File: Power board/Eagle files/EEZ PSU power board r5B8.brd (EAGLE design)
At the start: 74 x 150 mm, 270 parts, among them IC1 LTC3864, IC10 REF5025, IC11 DAC8552, IC12 ADG465SOT-23, IC13 TS5A9411DCKT, IC14 ADS1120, IC15 LP339D, IC2 MC79L05, IC3 MC78L05, IC4 LM5574, IC5 LP2951SO8, IC6 TL072D, IC7 TL072D, IC8 OP27GSZ, IC9 MCP23S08-E/SO, Q1 SUD19P06-60, Q10 MMBT5401, Q11 MMBT5401, Q12 MMBT5551, Q13 MMBT5551, Q14 BSS84P, Q15 2N7002, Q16 MMBT5551, Q17 MMBT5401, Q18 MMBT5551, Q19 MMBT5551, Q2 MMBT5401, Q3 2N7002, Q4 IRFP250N, Q5 BC857C, Q6 BC846C, Q7 BCP56-16.115, Q8 IRFR5410, Q9 BCP56-16.115, X1 282836-3, X2 282836-2, X3 SSW-113-02-T-D-RA

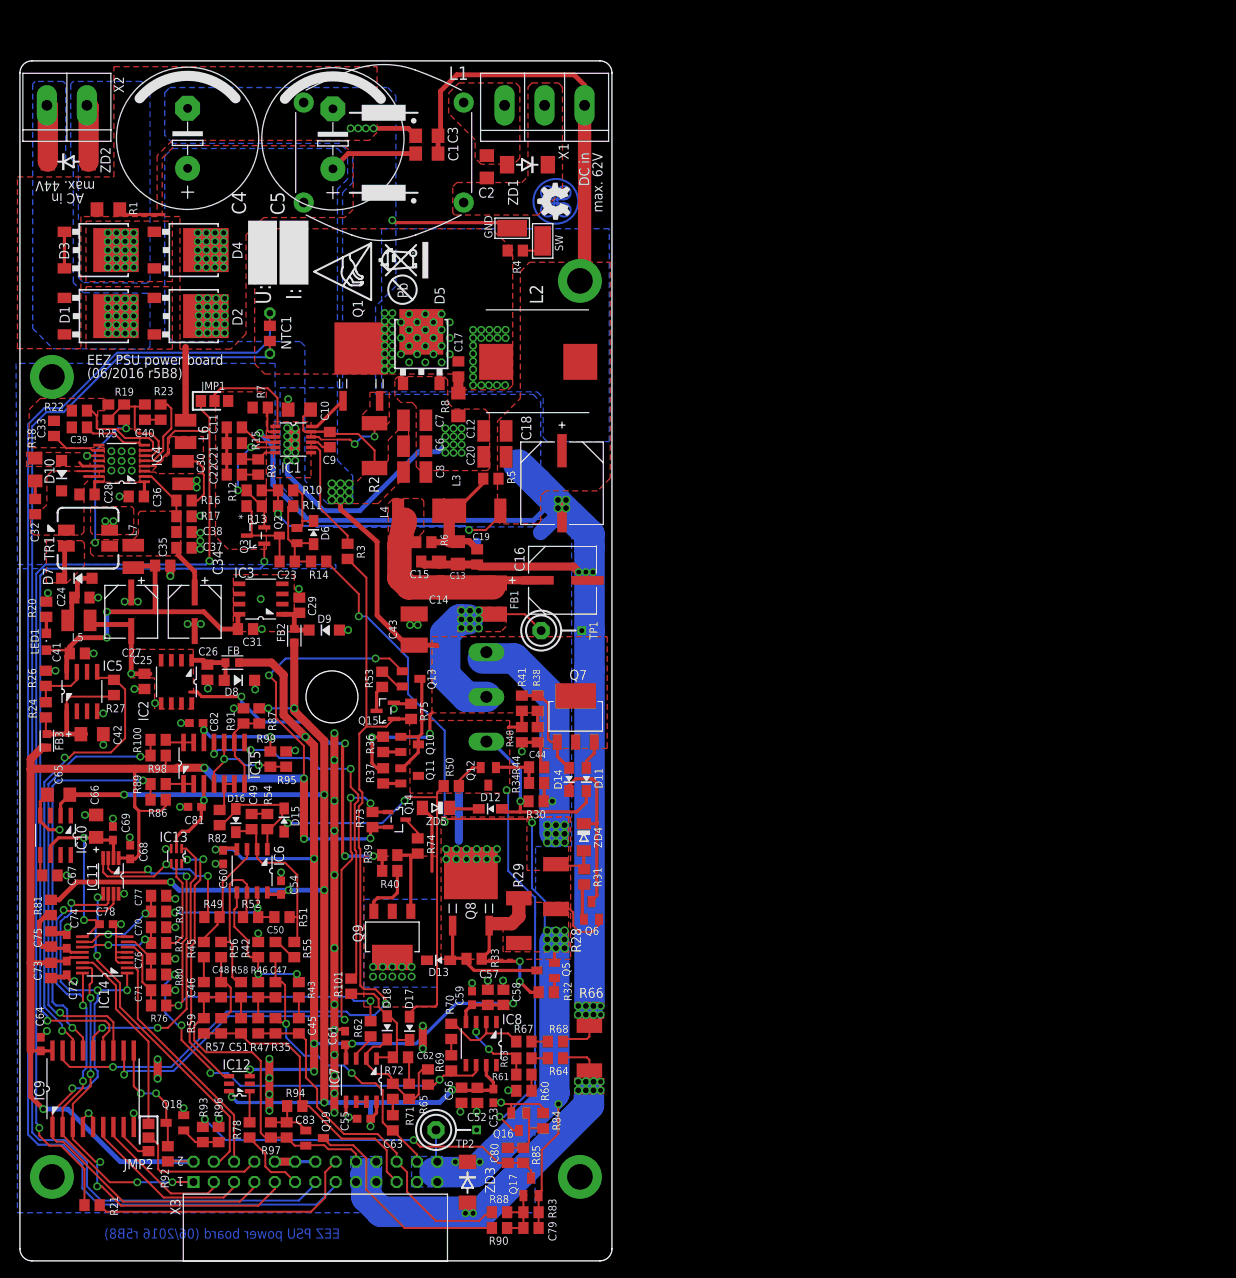
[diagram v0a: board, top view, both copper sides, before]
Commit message: Power board PCB layout and BOM changes
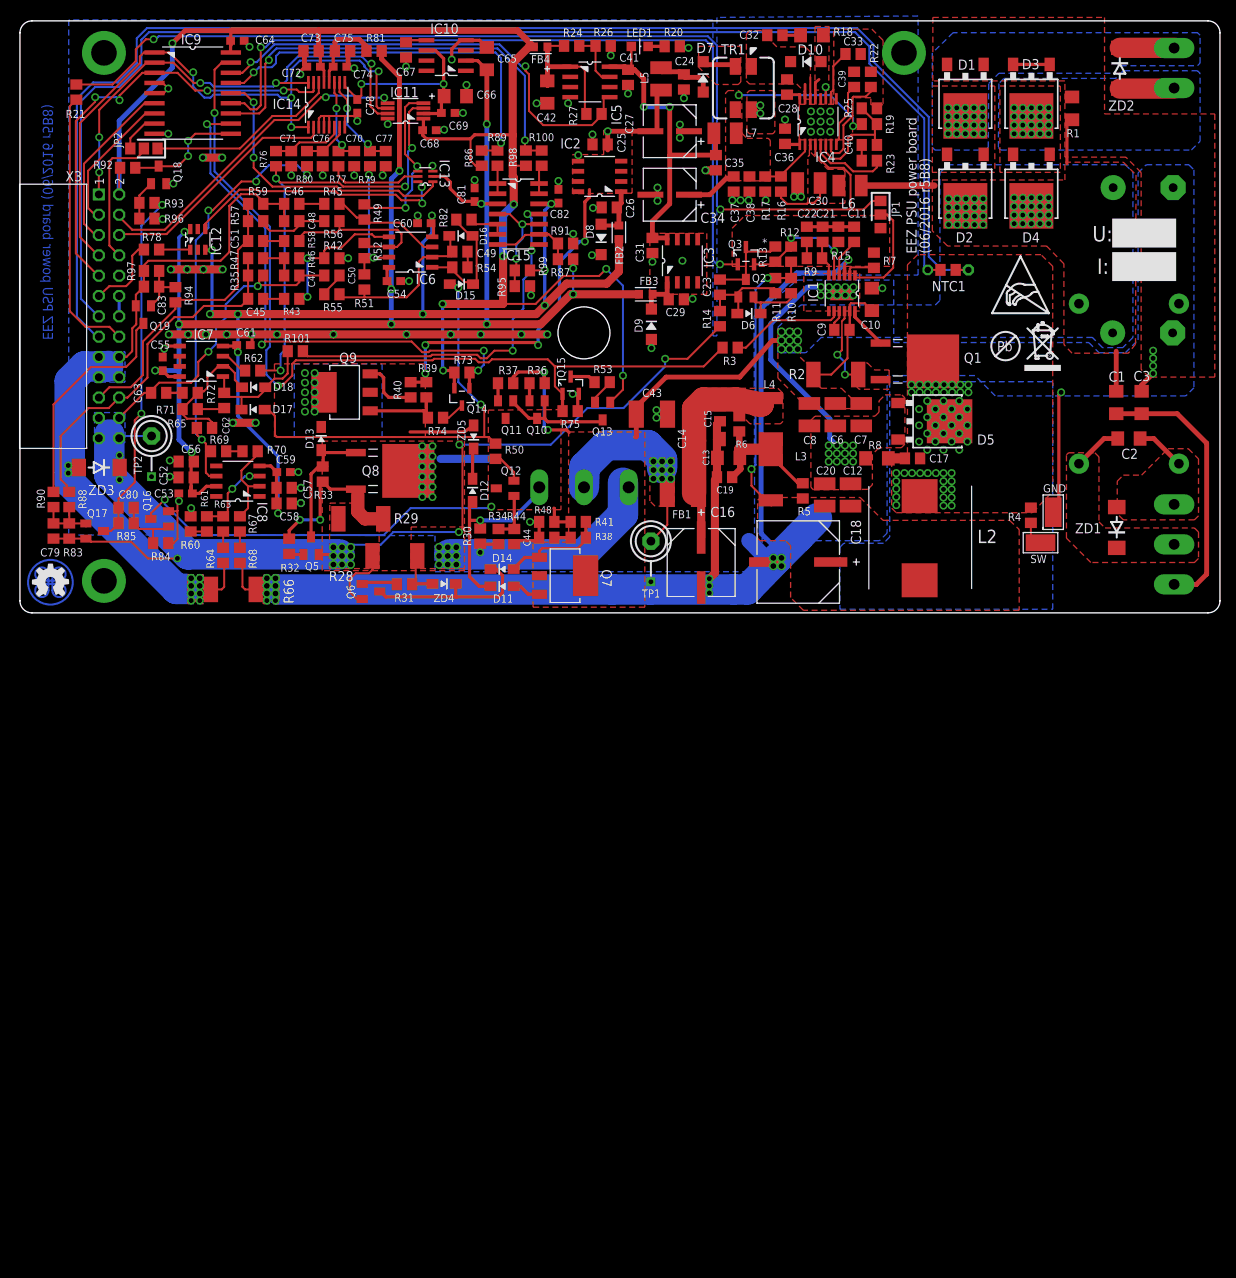
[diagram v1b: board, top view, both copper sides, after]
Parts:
- removed FB: 60R@100MHz, EEZ_Lib1:BEAD0603
- removed JMP1, JMP2: 0R-JUMPA, jump-0r-smd:A0R-JMP
- added FB4: 60R@100MHz, EEZ_Lib1:BEAD0603
- added JP1, JP2: 0R-JUMPA, jump-0r-smd:A0R-JMP
- C18: value EEEFK1J470P -> EEEFK1J101P
- D5: device EEZ_Lib1:TO252@1 -> EEZ_Lib1:TO252
- L2: value See Note 1.2 -> 7443551331
- LED1: device led:CHIPLED_0805 -> EEZ_Lib1:LED_0805
- R12: value See Note 1.3 -> 324K
- ZD4: value 13V -> BZX384-C15.115; device EEZ_Lib1:MINIMELF -> EEZ_Lib1:SOD323-W
- ZD5: value 6V2 -> PDZ6.2B; device EEZ_Lib1:MINIMELF -> EEZ_Lib1:SOD323-W
- moved X2 140.9 mm to (144.3, 141.6), flipped to the bottom, turned to 180 degrees
- moved R21 139.1 mm to (7.05, 141.1), turned to 270 degrees
- moved ZD2 132.0 mm to (137.5, 144.1), turned to 270 degrees
- moved C64 127.8 mm to (27.2, 147.5), turned to 0 degrees
- moved IC9 125.1 mm to (21.6, 141.0), turned to 0 degrees
- moved R92 123.4 mm to (13.5, 131.6), turned to 180 degrees
- moved R1 121.1 mm to (131.5, 139.1), turned to 90 degrees
- moved C4 119.6 mm to (140.4, 129.2), flipped to the bottom, turned to 180 degrees
- moved C73 119.4 mm to (36.4, 146.2), turned to 0 degrees
- moved Q18 118.5 mm to (17.3, 130.7), turned to 0 degrees
- moved C75 116.8 mm to (40.3, 146.2), turned to 180 degrees
- moved C72 116.8 mm to (36.7, 144.3), turned to 0 degrees
- moved D3 116.7 mm to (126.4, 139.1), turned to 180 degrees
- moved R93 116.7 mm to (15.9, 127.3), turned to 0 degrees
- moved R96 114.8 mm to (15.9, 125.3), turned to 180 degrees
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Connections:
- net !INT: now also JP2.2; no longer JMP2.2
- net !PS_DRDY: now also JP2.3; no longer JMP2.3
- net +5V: now also FB4.P$2; no longer FB3.P$2
- net AC_IN1: now also X2.1; no longer X2.2
- net AC_IN2: now also X2.2; no longer X2.1
- net DC+: now also L1.2; no longer L1.1
- net DC-: now also L1.1, X1.3; no longer L1.2, X1.1
- net DC_OUT: now also L1.3; no longer L1.4
- net EARTH: now also X1.1; no longer X1.3
- net GND: now also L1.4; no longer L1.3
- net INT_EXP: now also JP2.1; no longer JMP2.1
- net MODE: now also JP1.2; no longer JMP1.2
- net N$4: now also FB2.P$1; no longer FB.P$1
- net N$5: now also FB3.P$1; no longer FB2.P$1
- net N$6: now also FB4.P$1; no longer FB3.P$1
- net SGND: now also JP1.1; no longer JMP1.1
- net SYNC: now also JP1.3; no longer JMP1.3
- net V+: now also FB3.P$2; no longer FB2.P$2
- net V-: now also FB2.P$2; no longer FB.P$2
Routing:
- net EARTH: track 52.0 -> 33.8 mm, vias 1 -> 0
- net DC-: track 0.00 -> 6.15 mm
- net DC+: track 0.00 -> 6.15 mm
- net DC_OUT: track 84.2 -> 78.1 mm
- net GND: track 247.2 -> 241.5 mm
- net POUT-: track 107.6 -> 110.7 mm
- net AUX_USET_IN: track 9.05 -> 9.89 mm
- net +5V: track 189.5 -> 188.9 mm
- net Q4_OUT: track 41.6 -> 42.1 mm
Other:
- board size 74 x 150 mm -> 150 x 74 mm
- board text added: "AC in 1"
- board text added: "AC in 2"
- board text added: "AC input X2"
- board text added: "DC in max. 62V"
- board text added: "DC in+ 2"
- board text added: "DC in- 1"
- board text added: "DC input X1"
- board text added: "Earth 3"
- board text added: "FB4"
- board text added: "JP1"
- board text added: "JP2"
- board text removed: "DC in"
- board text removed: "FB"
- board text removed: "JMP1"
- board text removed: "JMP2"
- board text removed: "Licensed under the TAPR Open Hardware License (www.tapr.org/OHL)"
- board text removed: "max. 62V"

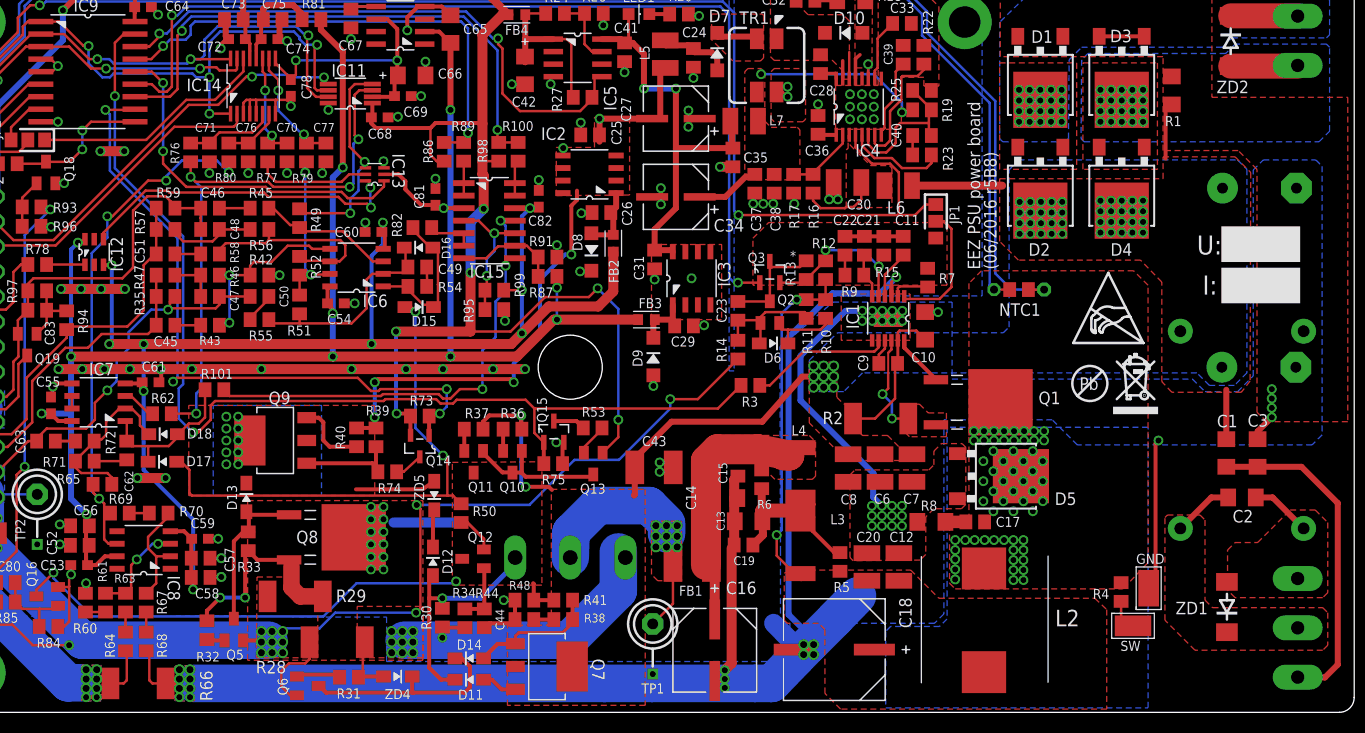
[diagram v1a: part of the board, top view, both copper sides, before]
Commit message: Missed hole added to Power board, minor bottom silk mask changes
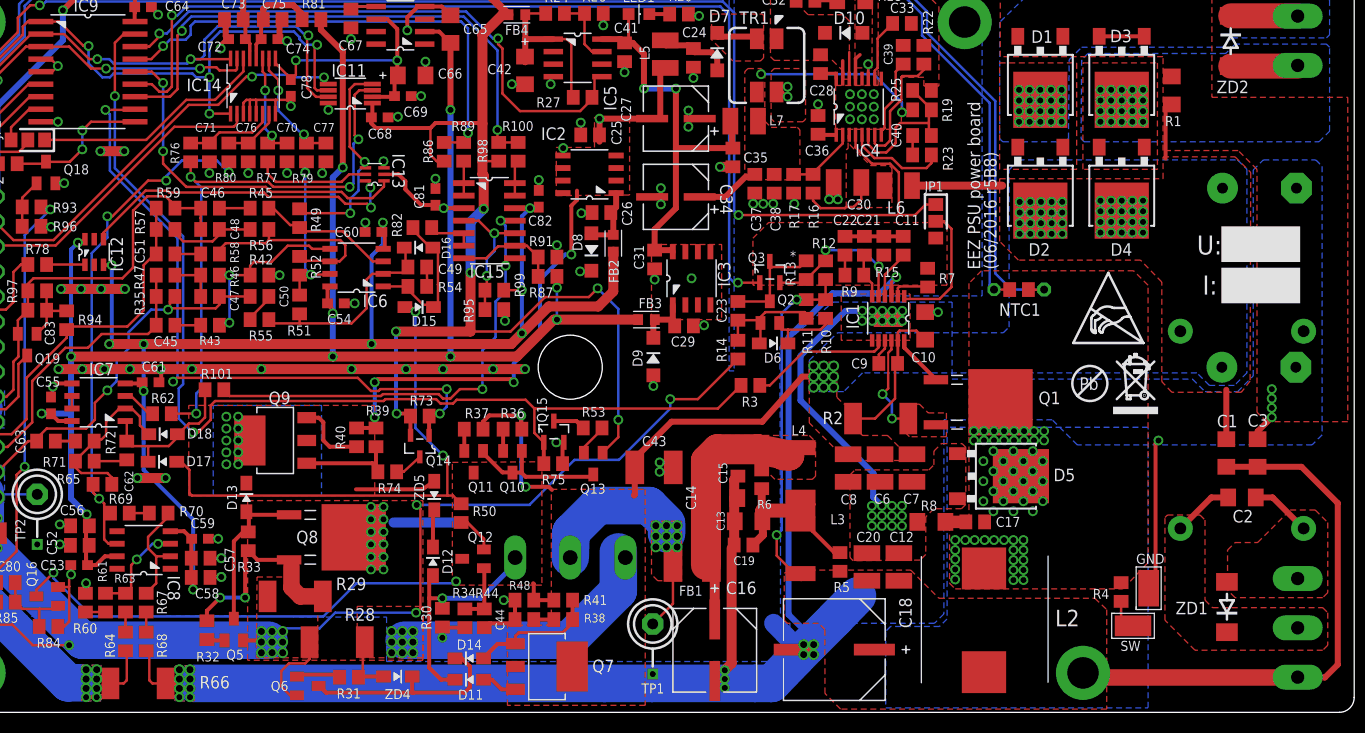
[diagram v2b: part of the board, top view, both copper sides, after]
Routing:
- net EARTH: track 33.8 -> 55.8 mm, vias 0 -> 1

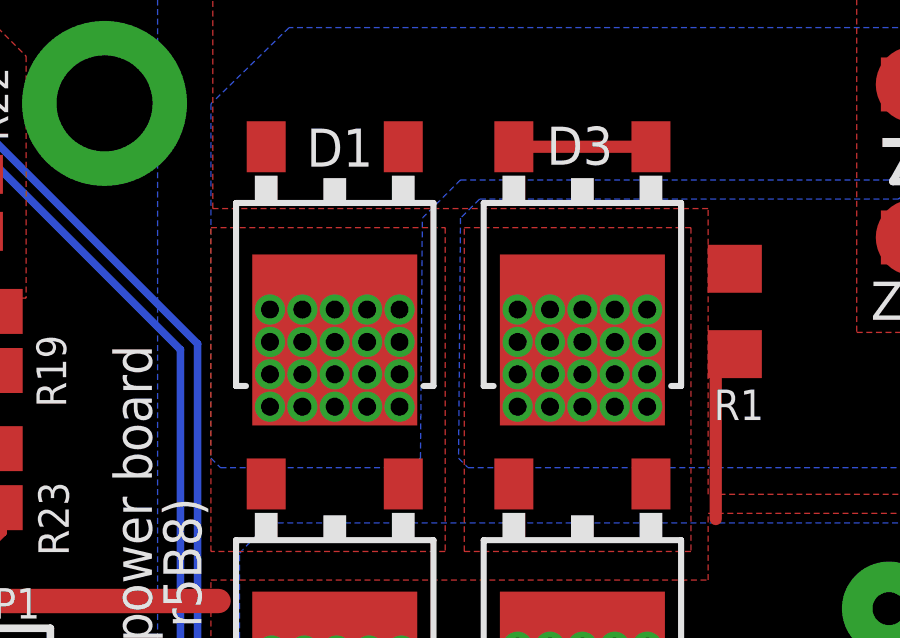
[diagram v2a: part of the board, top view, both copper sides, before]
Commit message: Consolidated BOM for PCBA, AUX PS BOM update, Power module PCB update
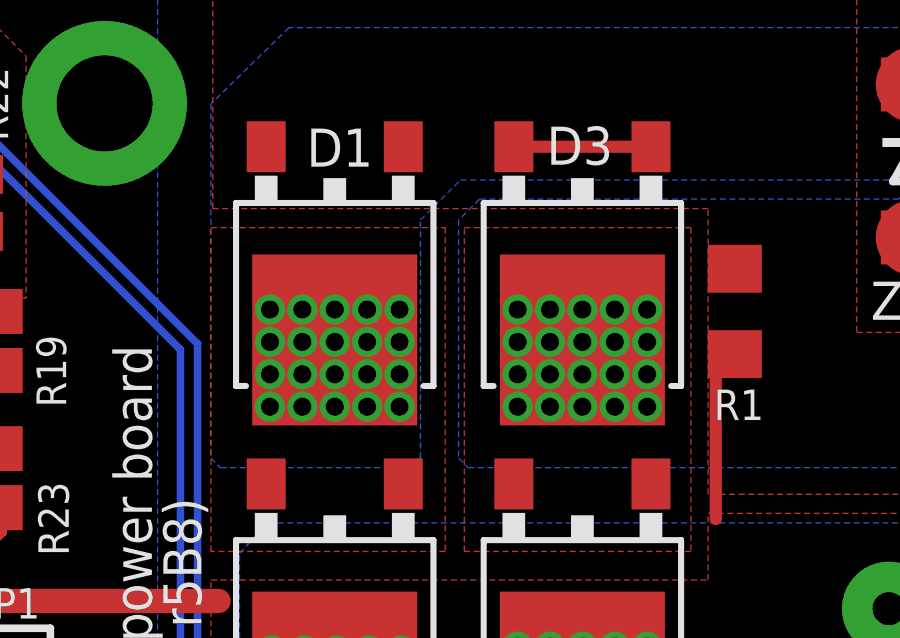
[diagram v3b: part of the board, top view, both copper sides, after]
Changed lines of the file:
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@@
 <layer number="27" name="tValues" color="10" fill="1" visible="no" active="yes"/>
 <layer number="28" name="bValues" color="11" fill="1" visible="no" active="yes"/>
-<layer number="29" name="tStop" color="7" fill="3" visible="no" active="yes"/>
-<layer number="30" name="bStop" color="7" fill="6" visible="yes" active="yes"/>
+<layer number="29" name="tStop" color="7" fill="3" visible="yes" active="yes"/>
+<layer number="30" name="bStop" color="7" fill="6" visible="no" active="yes"/>
 <layer number="31" name="tCream" color="7" fill="4" visible="no" active="yes"/>
 <layer number="32" name="bCream" color="7" fill="5" visible="no" active="yes"/>
@@
 <layer number="123" name="tTestmark" color="7" fill="1" visible="no" active="no"/>
 <layer number="124" name="bTestmark" color="7" fill="1" visible="no" active="no"/>
-<layer number="125" name="_tNames" color="14" fill="1" visible="yes" active="yes"/>
-<layer number="126" name="_bNames" color="5" fill="1" visible="yes" active="yes"/>
+<layer number="125" name="_tNames" color="14" fill="1" visible="no" active="yes"/>
+<layer number="126" name="_bNames" color="5" fill="1" visible="no" active="yes"/>
 <layer number="127" name="_tValues" color="7" fill="1" visible="no" active="no"/>
 <layer number="128" name="_bValues" color="7" fill="1" visible="no" active="no"/>
@@
 <vertex x="120.7135" y="133.858"/>
 <vertex x="121.031" y="134.1755"/>
-<vertex x="121.0945" y="142.1765"/>
+<vertex x="121.031" y="142.113"/>
 <vertex x="122.3645" y="143.4465"/>
 <vertex x="136.652" y="143.4465"/>
@@
 <vertex x="136.9695" y="142.8115"/>
 <vertex x="122.9995" y="142.8115"/>
-<vertex x="122.3645" y="142.1765"/>
+<vertex x="122.301" y="142.113"/>
 <vertex x="122.301" y="134.1755"/>
 <vertex x="122.6185" y="133.858"/>
